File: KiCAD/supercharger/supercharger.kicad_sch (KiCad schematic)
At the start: 13 parts, among them J2 BAT, J3 CALC, J4 UJC-H-G-SMT-1-P6-TR

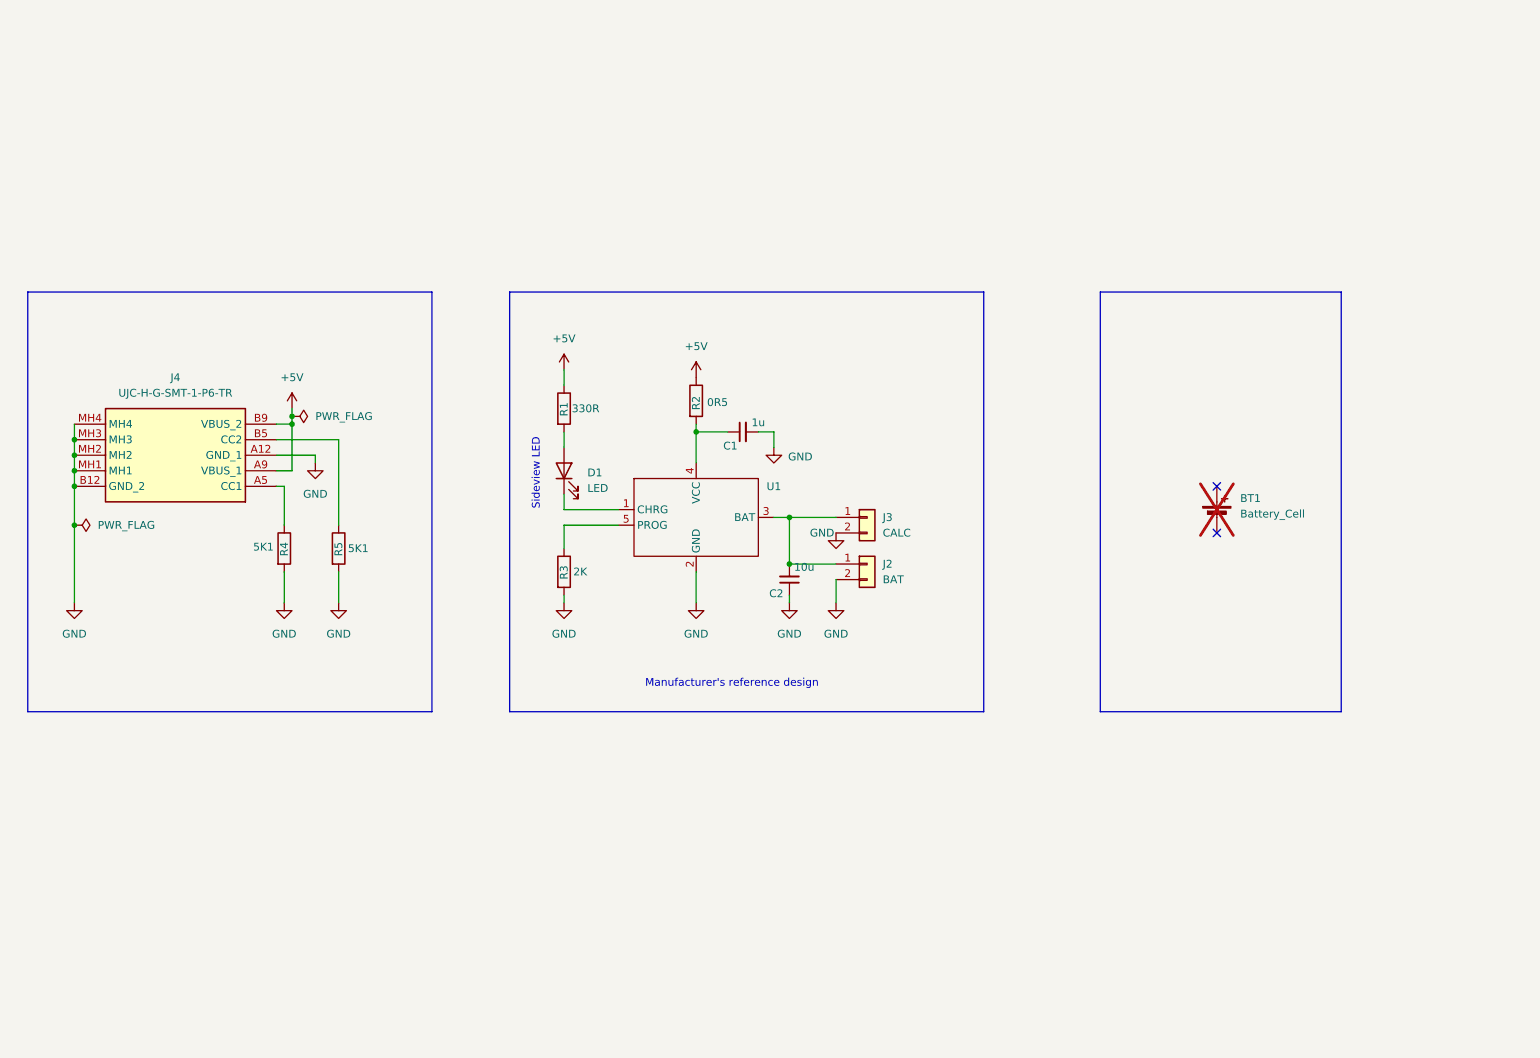
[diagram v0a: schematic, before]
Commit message: README.md update
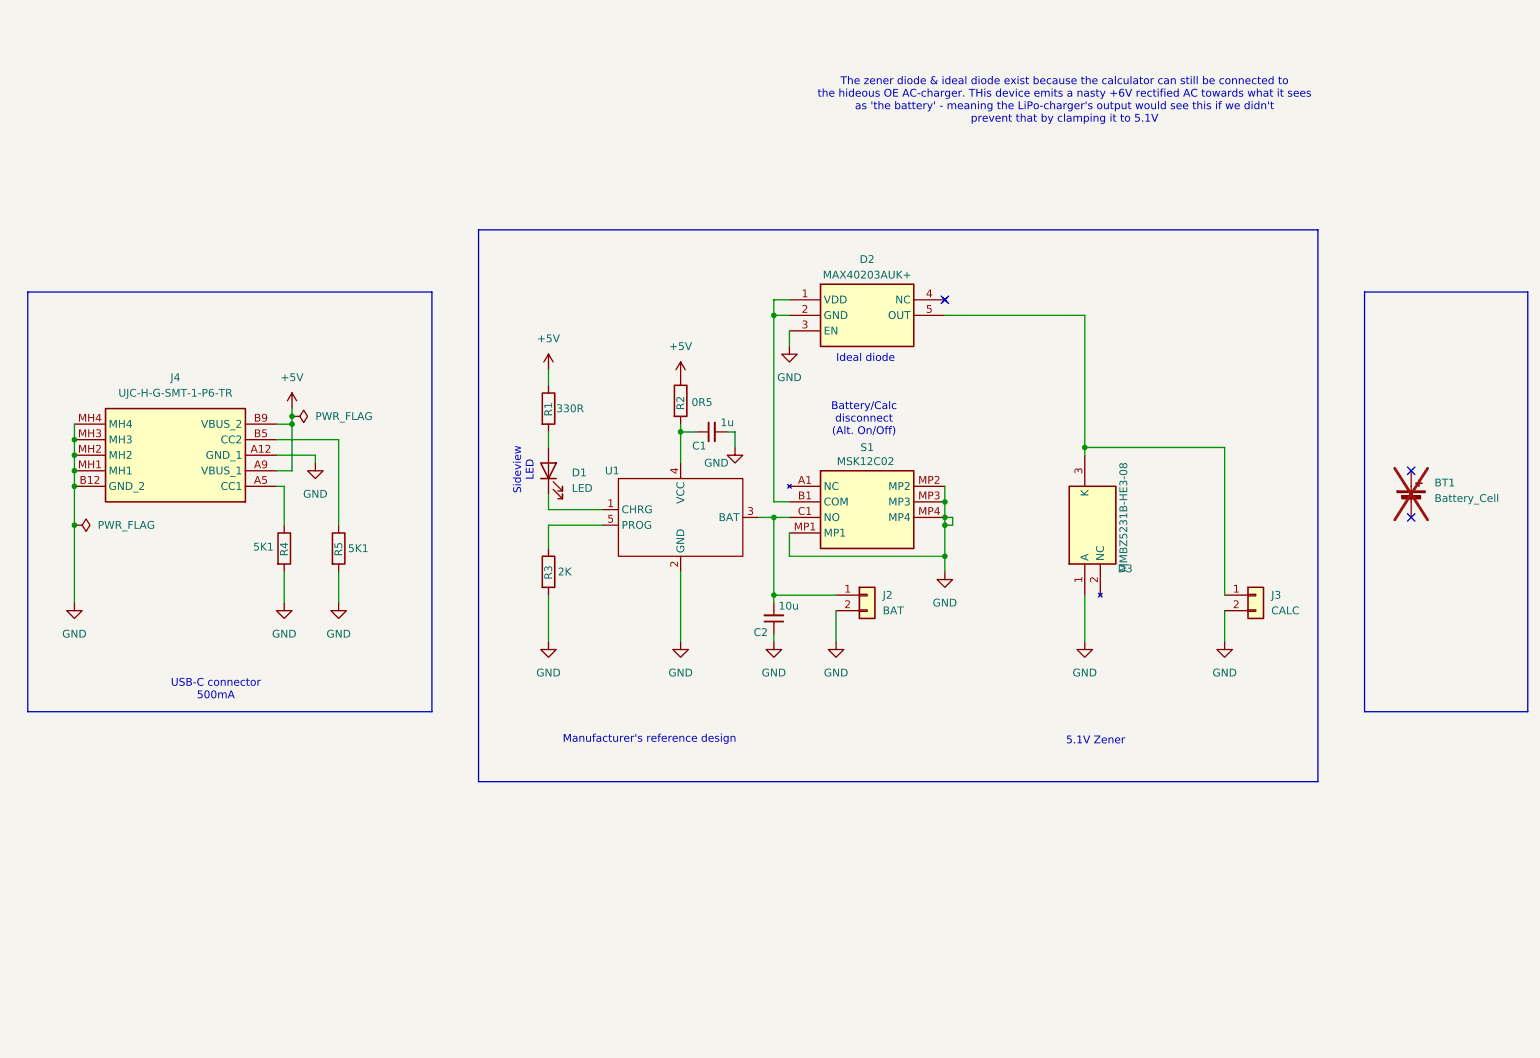
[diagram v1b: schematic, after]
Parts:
- added D2: MAX40203AUK+, SOT95P280X145-5N, symbol SamacSys_Parts:MAX40203AUK+
- added D3: MMBZ5231B-HE3-08, SOT95P248X115-3N, symbol SamacSys_Parts:MMBZ5231B-HE3-08
- added S1: MSK12C02, MSK12C02, symbol SamacSys_Parts:MSK12C02
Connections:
- net GND: now also D2.3 (EN), D3.1 (A), S1.MP1, S1.MP2, S1.MP3, S1.MP4
- net at C2.2, J2.1 (Pin_1), U1.3 (BAT): now also S1.C1 (NO); no longer J3.1 (Pin_1)
- new net: D2.1 (VDD), D2.2 (GND), S1.B1 (COM)
- new net: D2.5 (OUT), D3.3 (K), J3.1 (Pin_1)
- no-connect marks 2 -> 3
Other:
- note added: "5.1V Zener"
- note added: "Battery/Calc disconnect (Alt. On/Off)"
- note added: "Ideal diode"
- note added: "The zener diode & ideal diode exist because the calculator can still be connected to the hideous OE AC-charger. THis device emits a nasty +6V rectified AC towards what it sees as 'the battery' - meaning the LiPo-charger's output would see this if we didn't prevent that by clamping it to 5.1V"
- note added: "USB-C connector 500mA"
- moved on the sheet: BT1, C1, C2, D1, J2, J3, R1, R2, R3, U1

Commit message: Add buttons + charge display. Still need better/smaller connectors
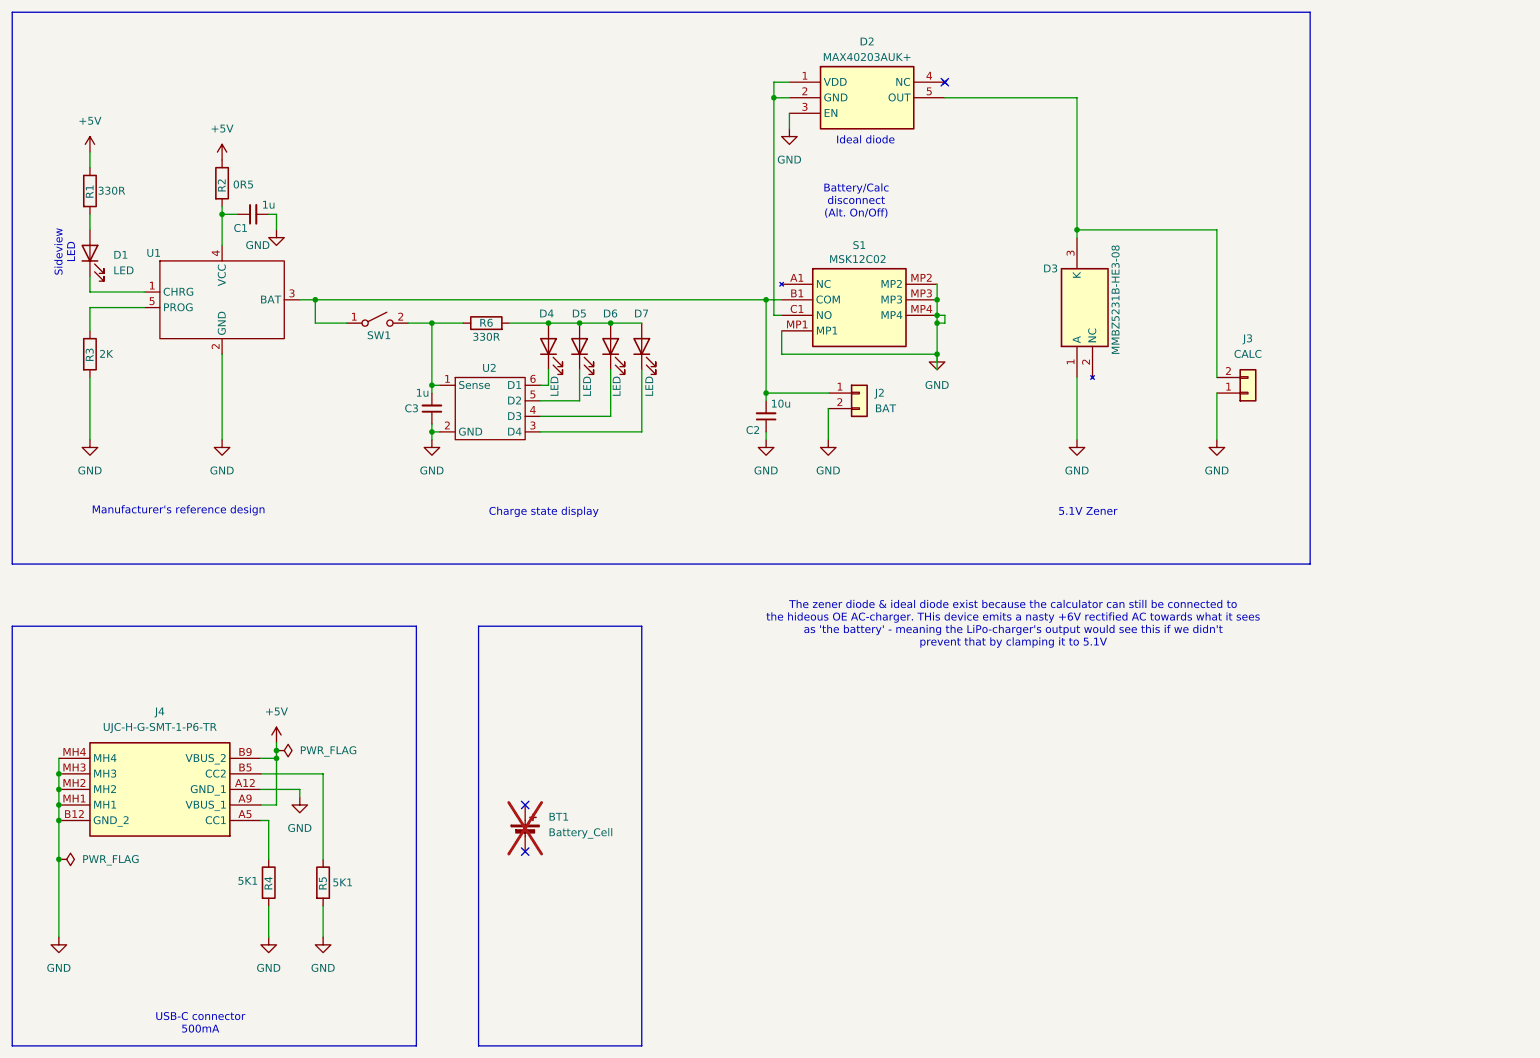
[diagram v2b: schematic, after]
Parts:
- added C3: 1u, Capacitor_SMD:C_0603_1608Metric, symbol Device:C_Small
- added D4, D5, D6, D7: LED, LED_SMD:LED_0603_1608Metric, symbol Device:LED
- added R6: 330R, Resistor_SMD:R_0603_1608Metric, symbol Device:R
- added SW1: SW_SPST, Button_Switch_SMD:SW_Push_1P1T-MP_NO_Horizontal_Alps_SKRTLAE010, symbol Switch:SW_SPST
- added U2: ~, Package_TO_SOT_SMD:TSOT-23-6_HandSoldering, symbol MFI_DIY_symbols:HM1160
- C1, C2: footprint Capacitor_SMD:C_0805_2012Metric_Pad1.18x1.45mm_HandSolder -> Capacitor_SMD:C_0603_1608Metric
- D1: footprint LED_SMD:LED_0805_2012Metric -> LED_SMD:LED_0603_1608Metric
- J3: footprint Connector_JST:JST_PH_S2B-PH-K_1x02_P2.00mm_Horizontal -> Connector_PinHeader_2.54mm:PinHeader_1x02_P2.54mm_Horizontal
- R1, R3, R4, R5: footprint Resistor_SMD:R_0805_2012Metric_Pad1.20x1.40mm_HandSolder -> Resistor_SMD:R_0603_1608Metric
- R2: footprint Resistor_SMD:R_0805_2012Metric_Pad1.20x1.40mm_HandSolder -> Resistor_SMD:R_0805_2012Metric
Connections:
- net GND: now also J3.1 (Pin_1), C3.1, U2.2 (GND); no longer J3.2 (Pin_2)
- net at D2.1 (VDD), D2.2 (GND): now also S1.C1 (NO); no longer S1.B1 (COM)
- net at D2.5 (OUT), D3.3 (K): now also J3.2 (Pin_2); no longer J3.1 (Pin_1)
- net at C2.2, J2.1 (Pin_1), U1.3 (BAT): now also S1.B1 (COM), SW1.1 (A); no longer S1.C1 (NO)
- new net: D4.1 (K), U2.6 (D1)
- new net: D4.2 (A), D5.2 (A), D6.2 (A), D7.2 (A), R6.2
- new net: C3.2, R6.1, SW1.2 (B), U2.1 (Sense)
- new net: D6.1 (K), U2.4 (D3)
- new net: D7.1 (K), U2.3 (D4)
- new net: D5.1 (K), U2.5 (D2)
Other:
- note added: "Charge state display"
- moved on the sheet: BT1, C1, C2, D1, D2, D3, J2, J3, J4, R1, R2, R3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

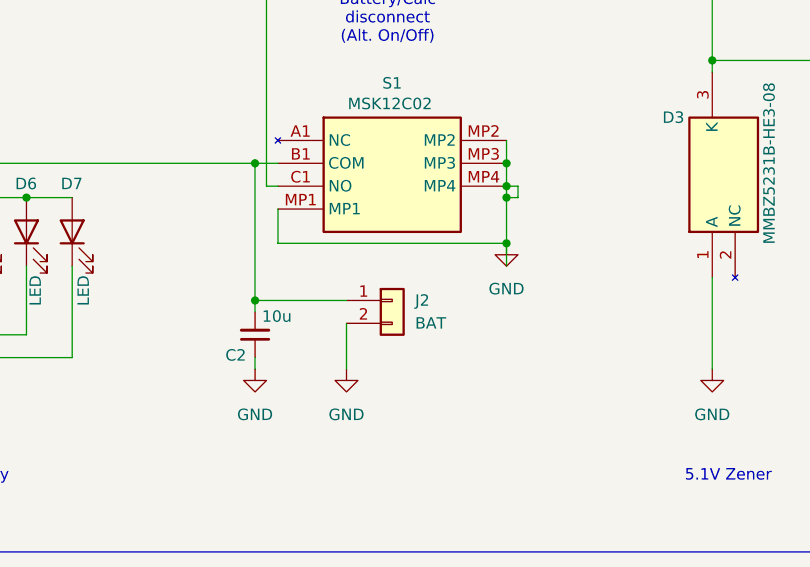
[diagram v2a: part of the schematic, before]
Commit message: Rearrange components, add the elusive JST 1.25mm 2-pole connector (DIY).
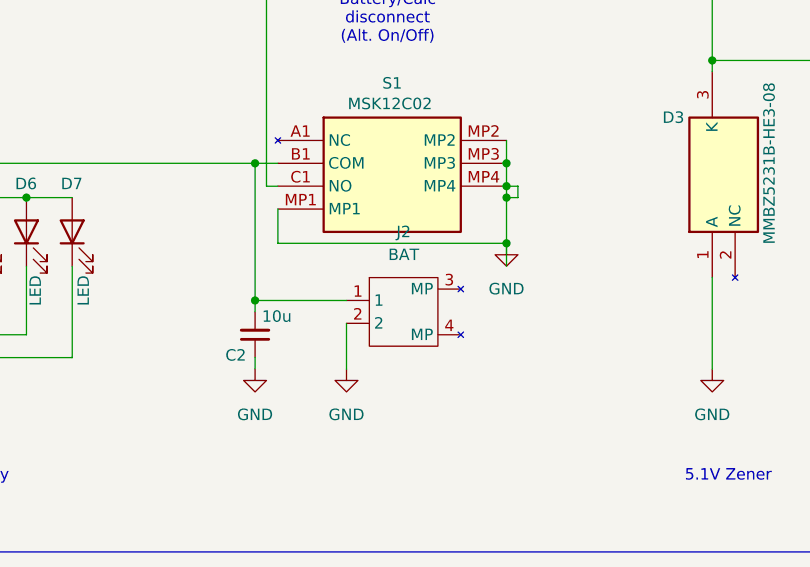
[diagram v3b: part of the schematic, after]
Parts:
- J2: footprint Connector_JST:JST_PH_S2B-PH-K_1x02_P2.00mm_Horizontal -> MFI_DIY_footprints:Connector JST PH 1.25mm horizontal; symbol Connector_Generic:Conn_01x02 -> MFI_DIY_symbols:JST_PH_2x1_1.25mm_horizontal
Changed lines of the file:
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@@
 	)
 	(symbol
-		(lib_id "Connector_Generic:Conn_01x02")
-		(at 158.75 82.55 0)
+		(lib_id "MFI_DIY_symbols:JST_PH_2x1_1.25mm_horizontal")
+		(at 160.02 83.82 0)
 		(unit 1)
 		(exclude_from_sim no)
@@
 		(fields_autoplaced yes)
 		(property "Reference" "J2"
-			(at 161.29 82.5499 0)
+			(at 160.02 74.93 0)
 			(effects
 				(font
 					(size 1.27 1.27)
 				)
-				(justify left)
 			)
 		)
 		(property "Value" "BAT"
-			(at 161.29 85.0899 0)
+			(at 160.02 77.47 0)
 			(effects
 				(font
 					(size 1.27 1.27)
 				)
-				(justify left)
 			)
 		)
-		(property "Footprint" "Connector_JST:JST_PH_S2B-PH-K_1x02_P2.00mm_Horizontal"
-			(at 158.75 82.55 0)
+		(property "Footprint" "MFI_DIY_footprints:Connector JST PH 1.25mm horizontal"
+			(at 160.02 78.74 0)
 			(effects
 				(font
@@
 		)
 		(property "Datasheet" "~"
-			(at 158.75 82.55 0)
+			(at 160.02 78.74 0)
 			(effects
 				(font
@@
 		)
 		(property "Description" "Generic connector, single row, 01x02, script generated (kicad-library-utils/schlib/autogen/connector/)"
-			(at 158.75 82.55 0)
+			(at 160.02 78.74 0)
 			(effects
 				(font
@@
 		(pin "2"
 		)
+		(pin "3"
+		)
+		(pin "4"
+		)
 		(instances

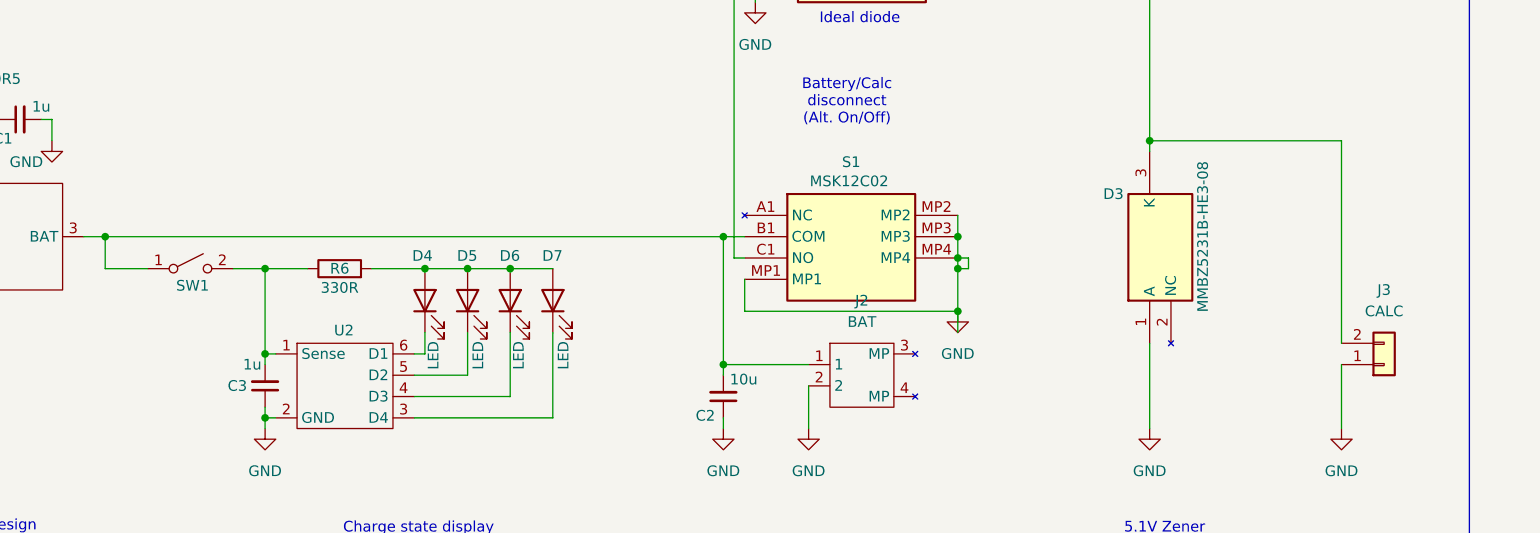
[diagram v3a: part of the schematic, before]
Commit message: Move USB-C towards side by 1mm, tweak component placement, Add lid and PCB dummies
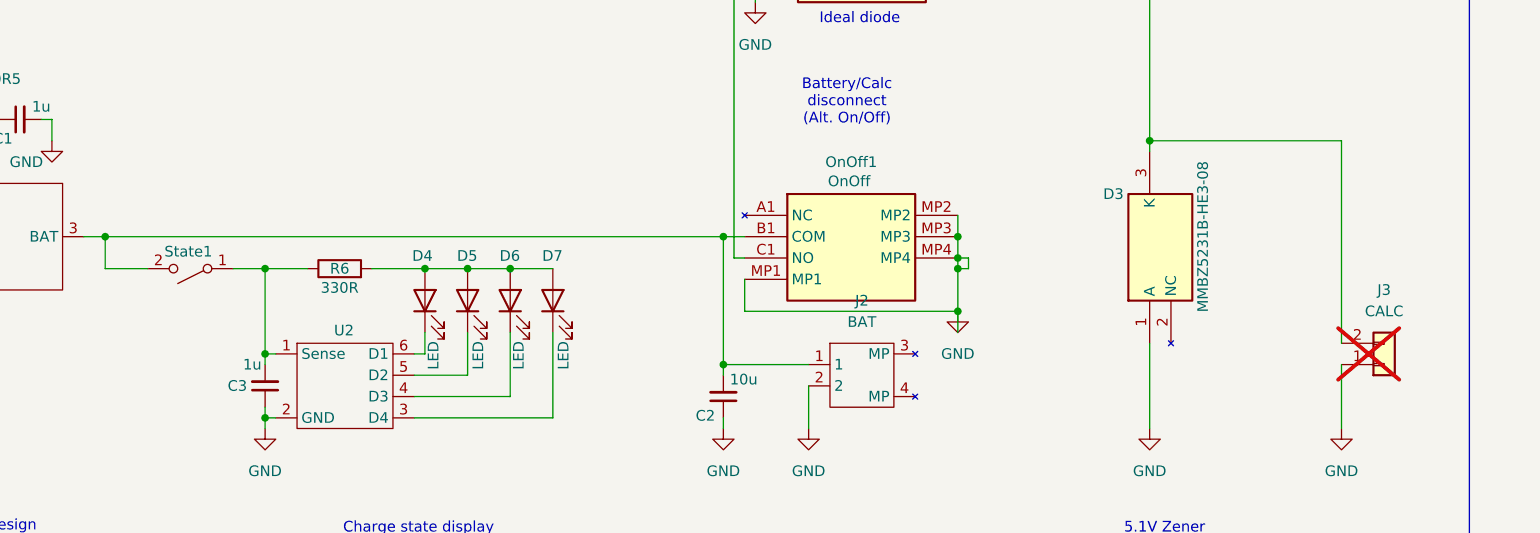
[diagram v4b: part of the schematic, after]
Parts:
- J3: now not fitted
- OnOff1: renamed from S1; value MSK12C02 -> OnOff
- State1: renamed from SW1; value SW_SPST -> State; footprint Button_Switch_SMD:SW_Push_1P1T-MP_NO_Horizontal_Alps_SKRTLAE010 -> EC-parts:B3U3000PMB
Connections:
- net at C2.2, J2.1, OnOff1.B1 (COM)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: now also State1.2 (B); no longer State1.1 (A)
- net at C3.2, R6.1, U2.1 (Sense): now also State1.1 (A); no longer State1.2 (B)
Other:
- moved on the sheet: State1
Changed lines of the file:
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@@
 		(in_bom yes)
 		(on_board yes)
-		(dnp no)
+		(dnp yes)
 		(property "Reference" "J3"
 			(at 222.25 73.66 0)
@@
 	(symbol
 		(lib_id "Switch:SW_SPST")
-		(at 80.01 71.12 0)
-		(unit 1)
-		(exclude_from_sim no)
-		(in_bom yes)
-		(on_board yes)
-		(dnp no)
-		(property "Reference" "SW1"
-			(at 80.264 73.152 0)
-			(effects
-				(font
-					(size 1.27 1.27)
-				)
-			)
-		)
-		(property "Value" "SW_SPST"
-			(at 80.01 67.31 0)
-			(effects
-				(font
-					(size 1.27 1.27)
-				)
-				(hide yes)
-			)
-		)
-		(property "Footprint" "Button_Switch_SMD:SW_Push_1P1T-MP_NO_Horizontal_Alps_SKRTLAE010"
+		(at 80.01 71.12 180)
+		(unit 1)
+		(exclude_from_sim no)
+		(in_bom yes)
+		(on_board yes)
+		(dnp no)
+		(property "Reference" "State1"
+			(at 79.756 69.088 0)
+			(effects
+				(font
+					(size 1.27 1.27)
+				)
+			)
+		)
+		(property "Value" "State"
+			(at 80.01 74.93 0)
+			(effects
+				(font
+					(size 1.27 1.27)
+				)
+				(hide yes)
+			)
+		)
+		(property "Footprint" "EC-parts:B3U3000PMB"
 			(at 80.01 71.12 0)
 			(effects
@@
 			(project ""
 				(path "/beb21a27-8a6b-49b9-b0ea-25f155128b2e"
-					(reference "SW1")
+					(reference "State1")
 					(unit 1)
 				)
@@
 		(on_board yes)
 		(dnp no)
-		(property "Reference" "S1"
+		(property "Reference" "OnOff1"
 			(at 158.75 58.42 0)
 			(effects
@@
 			)
 		)
-		(property "Value" "MSK12C02"
+		(property "Value" "OnOff"
 			(at 158.496 60.706 0)
 			(effects
@@
 			(project ""
 				(path "/beb21a27-8a6b-49b9-b0ea-25f155128b2e"
-					(reference "S1")
-					(unit 1)
-				)
+					(reference "OnOff1")
+					(unit 1)
+				)
